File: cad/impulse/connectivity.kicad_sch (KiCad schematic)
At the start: 4 parts

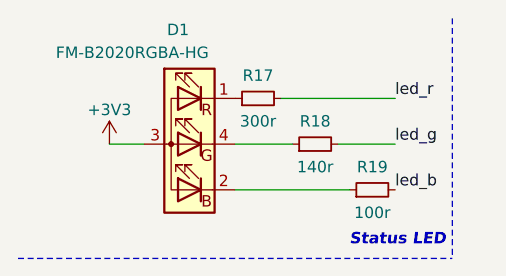
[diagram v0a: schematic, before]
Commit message: Transitioned to global labels when needed.
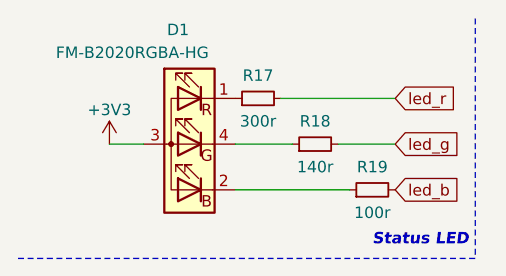
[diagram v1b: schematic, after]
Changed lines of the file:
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@@
     (stroke (width 0) (type default))
   )
-  (polyline (pts (xy 12.7 39.37) (xy 60.96 39.37))
+  (polyline (pts (xy 12.7 39.37) (xy 63.5 39.37))
     (stroke (width 0) (type dash))
   )
@@
     (stroke (width 0) (type default))
   )
-  (polyline (pts (xy 60.96 12.7) (xy 60.96 39.37))
+  (polyline (pts (xy 63.5 12.7) (xy 63.5 39.37))
     (stroke (width 0) (type dash))
   )
@@
     (stroke (width 0) (type default))
   )
-  (text "Status LED" (at 49.53 38.1 0)
+  (text "Status LED" (at 52.07 38.1 0)
     (effects (font (size 1.27 1.27) (thickness 0.254) bold italic) (justify left bottom))
   )
-  (label "led_g" (at 54.61 26.67 0) (fields_autoplaced)
-    (effects (font (size 1.27 1.27)) (justify left bottom))
+  (global_label "led_b" (shape input) (at 54.61 31.75 0) (fields_autoplaced)
+    (effects (font (size 1.27 1.27)) (justify left))
+    (property "Intersheetrefs" "${INTERSHEET_REFS}" (at 62.5352 31.75 0)
+      (effects (font (size 1.27 1.27)) (justify left) hide)
+    )
   )
-  (label "led_b" (at 54.61 31.75 0) (fields_autoplaced)
-    (effects (font (size 1.27 1.27)) (justify left bottom))
+  (global_label "led_g" (shape input) (at 54.61 26.67 0) (fields_autoplaced)
+    (effects (font (size 1.27 1.27)) (justify left))
+    (property "Intersheetrefs" "${INTERSHEET_REFS}" (at 62.5352 26.67 0)
+      (effects (font (size 1.27 1.27)) (justify left) hide)
+    )
   )
-  (label "led_r" (at 54.61 21.59 0) (fields_autoplaced)
-    (effects (font (size 1.27 1.27)) (justify left bottom))
+  (global_label "led_r" (shape input) (at 54.61 21.59 0) (fields_autoplaced)
+    (effects (font (size 1.27 1.27)) (justify left))
+    (property "Intersheetrefs" "${INTERSHEET_REFS}" (at 62.1724 21.59 0)
+      (effects (font (size 1.27 1.27)) (justify left) hide)
+    )
   )
   (symbol (lib_id "Device:R_Small") (at 52.07 31.75 90) (unit 1)

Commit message: Finished with LoRa.
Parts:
- added C15, C16, C35: 100n, symbol Device:C_Small
- added C17: 1n, symbol Device:C_Small
- added C18: 82p, symbol Device:C_Small
- added C19: 47n, symbol Device:C_Small
- added C20: 3p6, symbol Device:C_Small
- added C21, C28, C29, C33: 0f, symbol Device:C_Small
- added C22, C26: 100p, symbol Device:C_Small
- added C23, C30: 4p7, symbol Device:C_Small
- added C24: 12p, symbol Device:C_Small
- added C25: 8p2, symbol Device:C_Small
- added C27: 10n, symbol Device:C_Small
- added C31: 1p, symbol Device:C_Small
- added C32: 3p9, symbol Device:C_Small
- added C34: 470n, symbol Device:C_Small
- added C36, C37: C_Small, symbol Device:C_Small
- added J11: Micro_SD_Card, symbol Connector:Micro_SD_Card
- added J12: Conn_Coaxial, symbol Connector:Conn_Coaxial
- added L3: 56n, symbol Device:L_Small
- added L4: 8n2, symbol Device:L_Small
- added L5: 18n, symbol Device:L_Small
- added L6: 0n, symbol Device:L_Small
- added L7: 0h, symbol Device:L_Small
- added L8: 33n, symbol Device:L_Small
- added L9: 15u, symbol Device:L_Small
- added R25, R26, R27, R28: 10k, symbol Device:R_Small
- added R31: 100r, symbol Device:R_Small
- added U6: W25Q32JVSS, Package_SO:SOIC-8_5.23x5.23mm_P1.27mm, symbol Memory_Flash:W25Q32JVSS
- added U7: BGS12PL6, symbol impulse:BGS12PL6
- added U8: SX1268, symbol impulse:sx1268
- added Y1: 32MHZ, symbol Device:Crystal_GND24
- renumbered D1 to D6, R17 to R24, R18 to R29, R19 to R30
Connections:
- net +3V3: now also C15.1, C16.1, C27.1, C33.1, C35.1, J11.4 (VDD), L7.1, R25.1, R26.1, R27.1, R28.1, U6.8 (VCC), U7.4 (VDD), U8.1 (VDD_IN), U8.10 (VBAT), U8.11 (VBAT_IO)
- new net: C20.2, C24.1, L4.2, L5.1
- new net: C22.1, L5.2
- new net: C18.1, C19.1, L3.1, U8.24 (VR_PA)
- new net: C21.1, L3.2, U8.23 (RFO)
- new net: C20.1, C21.2, C23.1, L4.1
- new net: C34.1, L7.2, L9.1, U8.7 (VREG)
- new net: L9.2, U8.9 (DCC_SW)
- new net: C17.1, R31.2, U7.6 (CTRL)
- new net: C30.1, L8.1, U8.22 (RFI_N)
- new net: C32.1, L8.2, U8.21 (RFI_P)
- new net: C30.2, C31.1, U7.3 (RF1)
- new net: C26.2, C28.2, L6.1
- new net: C29.1, J12.1 (In), L6.2
- new net: C22.2, C25.1, U7.1 (RF2)
- new net: C26.1, U7.5 (RFIN)
- new net GND: C15.2, C16.2, C17.2, C18.2, C19.2, C23.2, C24.2, C25.2, C27.2, C28.1, C29.2, C31.2, C32.2, C33.2, C34.2, C35.2, C36.2, C37.2, J11.6 (VSS), J12.2 (Ext), U6.4 (GND), U7.2 (GND), U8.2 (GND), U8.20 (GND), U8.25 (GND), U8.5 (GND), U8.8 (GND), Y1.2, Y1.4
- new net SD_cs: J11.2 (DAT3/CD), R25.2
- new net SD_miso: J11.7 (DAT0), R28.2
- new net SD_mosi: J11.3 (CMD), R26.2
- new net SD_sck: J11.5 (CLK), R27.2
- new net flash_cs: U6.1 (~{CS})
- new net flash_miso: U6.2 (DO(IO1))
- new net flash_mosi: U6.5 (DI(IO0))
- new net flash_sck: U6.6 (CLK)
- new net sx_busy: U8.14 (BUSY)
- new net sx_dio_2: R31.1, U8.12 (DIO2)
- new net sx_miso: U8.16 (MISO)
- new net sx_mosi: U8.17 (MOSI)
- new net sx_nrst: U8.15 (NRESET)
- new net sx_nss: U8.19 (NSS)
- new net sx_sck: U8.18 (SCK)
- new net sx_xta: C37.1, U8.3 (XTA), Y1.3
- new net sx_xtb: C36.1, U8.4 (XTB), Y1.1
- no-connect marks 0 -> 7
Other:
- note added: "Flash Memory"
- note added: "LoRa Radio"
- note added: "SD Card"

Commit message: Finnished the design.
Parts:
- C36, C37: value C_Small -> 16p
- L6: value 0n -> 0h
- U6: footprint Package_SO:SOIC-8_5.23x5.23mm_P1.27mm -> (none)
- Y1: value 32MHZ -> XL7EL89COI-111YLC-32M
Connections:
- net sx_busy: no longer names the net of U8.14 (BUSY)
- net sx_nrst: no longer names the net of U8.15 (NRESET)
- no-connect marks 7 -> 9
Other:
- note added: "SPI1"
- note added: "SPI2"
- note added: "SPI3"
- company: (none) -> markbel
- title: (none) -> Connectivity
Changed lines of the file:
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@@
 (kicad_sch (version 20230121) (generator eeschema)
   (paper "A4")
+  (title_block
+    (title "Connectivity")
+    (company "markbel")
+  )
   (junction (at 128.27 91.44) (diameter 0) (color 0 0 0 0)
   )
@@
   )
   (no_connect (at 107.95 26.67))
+  (no_connect (at 106.68 109.22))
   (no_connect (at 107.95 44.45))
   (no_connect (at 31.75 60.96))
@@
   (no_connect (at 76.2 99.06))
   (no_connect (at 31.75 63.5))
+  (no_connect (at 106.68 111.76))
   (wire (pts (xy 229.87 85.09) (xy 233.68 85.09))
     (stroke (width 0) (type default))
@@
     (stroke (width 0) (type default))
   )
+  (text "SPI2" (at 58.42 74.93 0)
+    (effects (font (size 1.27 1.27) (thickness 0.254) bold italic) (justify left bottom))
+  )
+  (text "SPI3\n" (at 161.29 52.07 0)
+    (effects (font (size 1.27 1.27) (thickness 0.254) bold italic) (justify left bottom))
+  )
   (text "LoRa Radio" (at 273.05 109.22 0)
     (effects (font (size 1.27 1.27) (thickness 0.254) bold italic) (justify left bottom))
   )
   (text "Status LED" (at 52.07 38.1 0)
+    (effects (font (size 1.27 1.27) (thickness 0.254) bold italic) (justify left bottom))
+  )
+  (text "SPI1" (at 279.4 106.68 0)
     (effects (font (size 1.27 1.27) (thickness 0.254) bold italic) (justify left bottom))
   )
@@
     )
   )
-  (global_label "sx_busy" (shape input) (at 106.68 111.76 0) (fields_autoplaced)
-    (effects (font (size 1.27 1.27)) (justify left))
-    (property "Intersheetrefs" "${INTERSHEET_REFS}" (at 116.9033 111.76 0)
-      (effects (font (size 1.27 1.27)) (justify left) hide)
-    )
-  )
   (global_label "led_g" (shape input) (at 54.61 26.67 0) (fields_autoplaced)
     (effects (font (size 1.27 1.27)) (justify left))
@@
     )
   )
-  (global_label "sx_nrst" (shape input) (at 106.68 109.22 0) (fields_autoplaced)
-    (effects (font (size 1.27 1.27)) (justify left))
-    (property "Intersheetrefs" "${INTERSHEET_REFS}" (at 116.2986 109.22 0)
-      (effects (font (size 1.27 1.27)) (justify left) hide)
-    )
-  )
   (global_label "led_r" (shape input) (at 54.61 21.59 0) (fields_autoplaced)
     (effects (font (size 1.27 1.27)) (justify left))
@@
       (effects (font (size 1.27 1.27)) (justify left))
     )
-    (property "Footprint" "Package_SO:SOIC-8_5.23x5.23mm_P1.27mm" (at 41.91 58.42 0)
+    (property "Footprint" "" (at 41.91 58.42 0)
       (effects (font (size 1.27 1.27)) hide)
     )
@@
       (effects (font (size 1.27 1.27)) (justify left))
     )
-    (property "Value" "C_Small" (at 176.53 117.4813 0)
+    (property "Value" "16p" (at 176.53 117.4813 0)
       (effects (font (size 1.27 1.27)) (justify left))
     )
@@
   (symbol (lib_id "Device:Crystal_GND24") (at 166.37 113.03 0) (unit 1)
     (in_bom yes) (on_board yes) (dnp no)
-    (property "Reference" "Y1" (at 157.48 104.14 0)
-      (effects (font (size 1.27 1.27)))
-    )
-    (property "Value" "32MHZ" (at 157.48 106.68 0)
+    (property "Reference" "Y1" (at 160.02 106.68 0)
+      (effects (font (size 1.27 1.27)))
+    )
+    (property "Value" "XL7EL89COI-111YLC-32M " (at 149.86 109.22 0)
       (effects (font (size 1.27 1.27)))
     )
@@
       (effects (font (size 1.27 1.27)))
     )
-    (property "Value" "0n" (at 240.03 82.55 90)
+    (property "Value" "0h" (at 240.03 82.55 90)
       (effects (font (size 1.27 1.27)))
     )
@@
       (effects (font (size 1.27 1.27)) (justify left))
     )
-    (property "Value" "C_Small" (at 156.21 117.4813 0)
-      (effects (font (size 1.27 1.27)) (justify left))
-    )
+    (property "Value" "16p" (at 156.21 117.4813 0)
+      (effects (font (size 1.27 1.27)) (justify left))
+    )

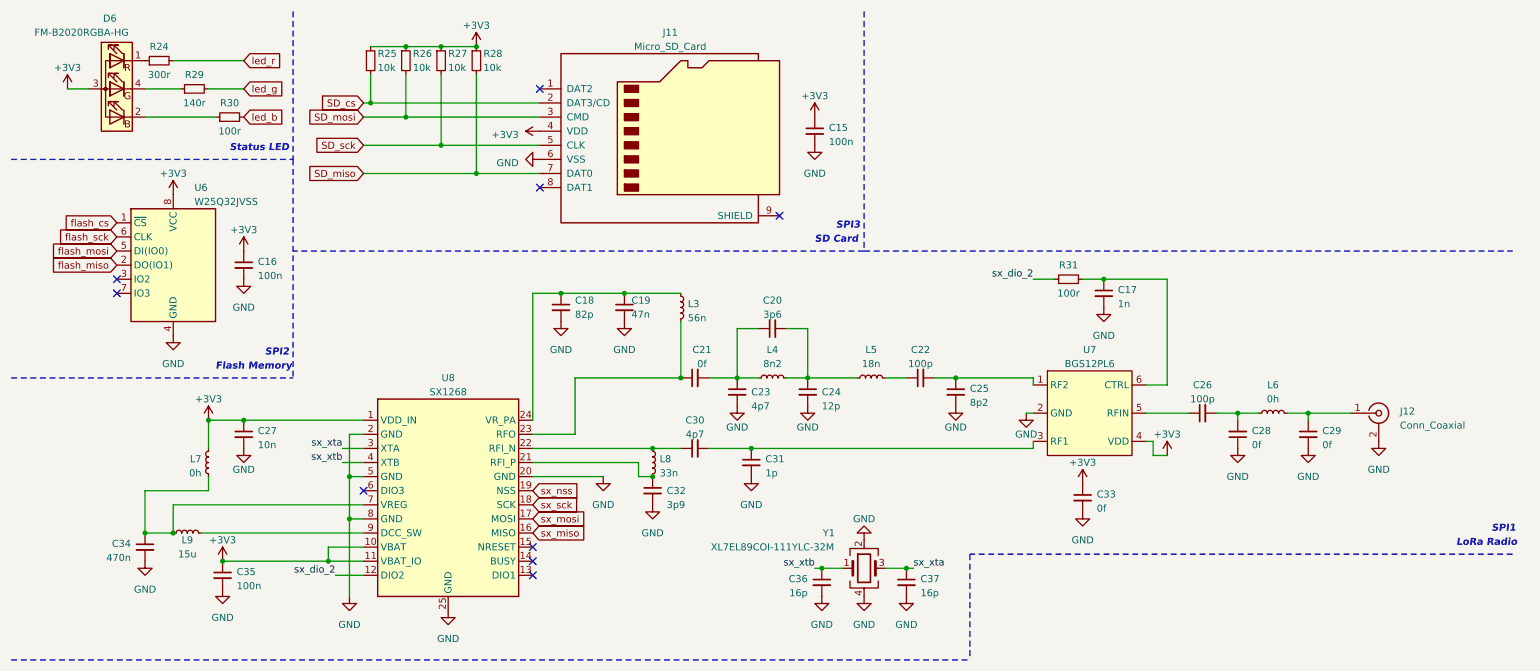
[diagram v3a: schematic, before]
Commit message: Started working on BOM, did consolidation.
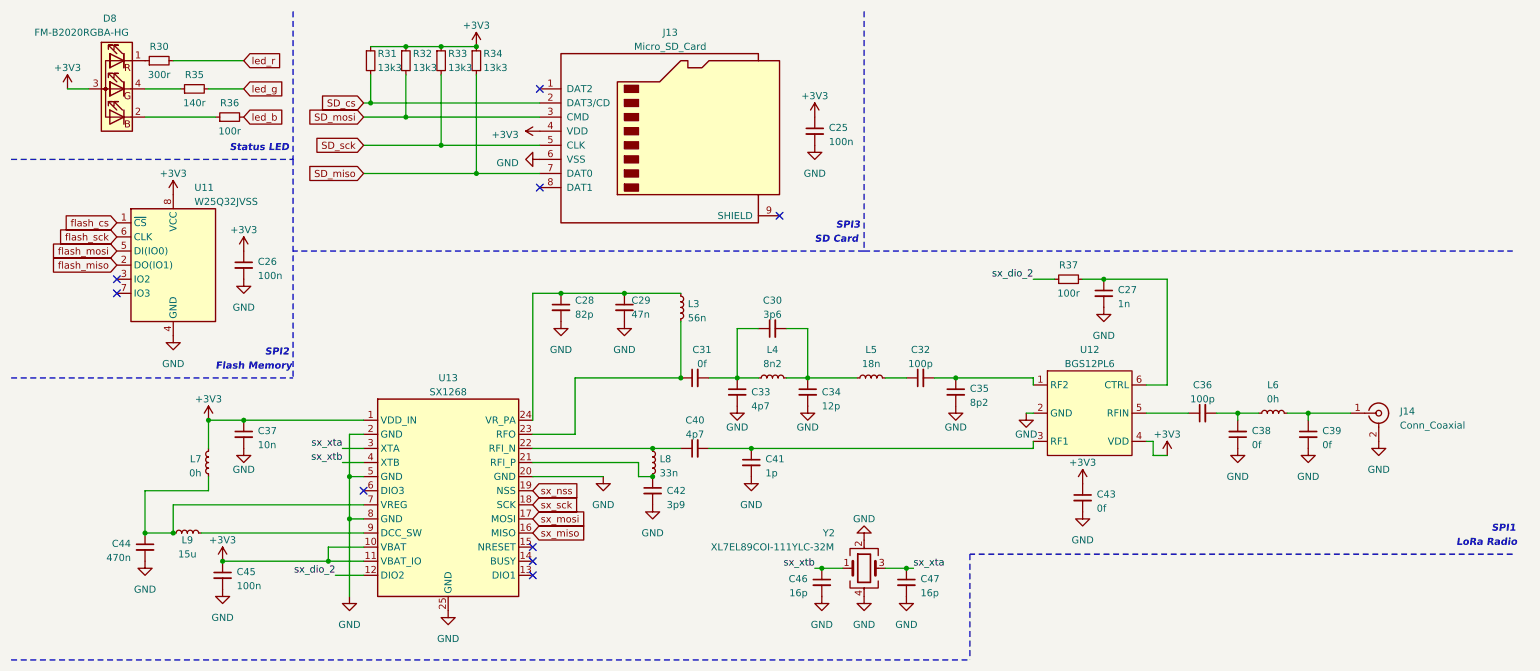
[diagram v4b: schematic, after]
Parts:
- C25: renamed from C15; lcsc (none) -> C1525
- C26: renamed from C16; lcsc (none) -> C1525
- C45: renamed from C35; lcsc (none) -> C1525
- C46: renamed from C36; lcsc (none) -> C5142569
- C47: renamed from C37; lcsc (none) -> C5142569
- D8: renamed from D6; lcsc (none) -> C108793
- J13: renamed from J11; lcsc (none) -> C393941
- J14: renamed from J12; lcsc (none) -> C5299419
- R30: renamed from R24; lcsc (none) -> C3017471
- R31: renamed from R25; value 10k -> 13k3; lcsc (none) -> C3015832
- R32: renamed from R26; value 10k -> 13k3; lcsc (none) -> C3015832
- R33: renamed from R27; value 10k -> 13k3; lcsc (none) -> C3015832
- R34: renamed from R28; value 10k -> 13k3; lcsc (none) -> C3015832
- R35: renamed from R29; lcsc (none) -> C3015963
- R36: renamed from R30; lcsc (none) -> C3152058
- R37: renamed from R31; lcsc (none) -> C3152058
- U11: renamed from U6; lcsc (none) -> C2834491
- U12: renamed from U7; lcsc (none) -> C2939943
- U13: renamed from U8; lcsc (none) -> C244368
- Y2: renamed from Y1; lcsc (none) -> C2965584
- renumbered C17 to C27, C18 to C28, C19 to C29, C20 to C30, C21 to C31, C22 to C32, C23 to C33, C24 to C34, C25 to C35, C26 to C36, C27 to C37, C28 to C38, C29 to C39, C30 to C40, C31 to C41, C32 to C42, C33 to C43, C34 to C44

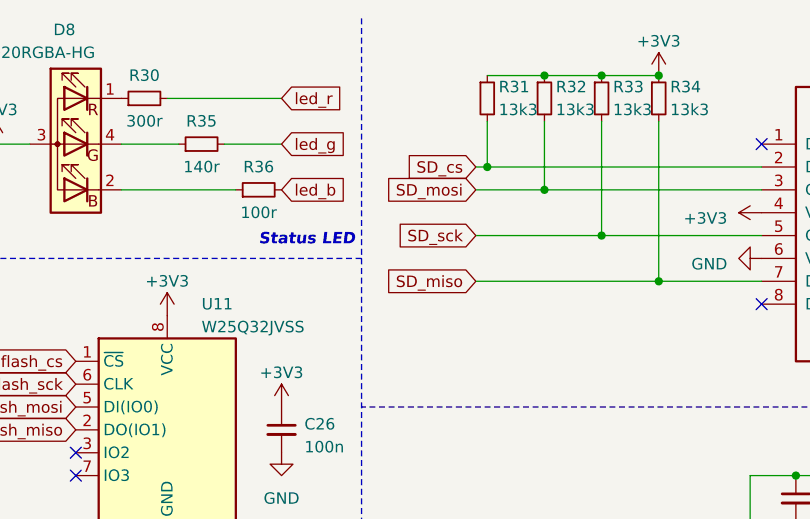
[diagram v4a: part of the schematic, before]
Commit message: Finished with schematic, starting to route traces.
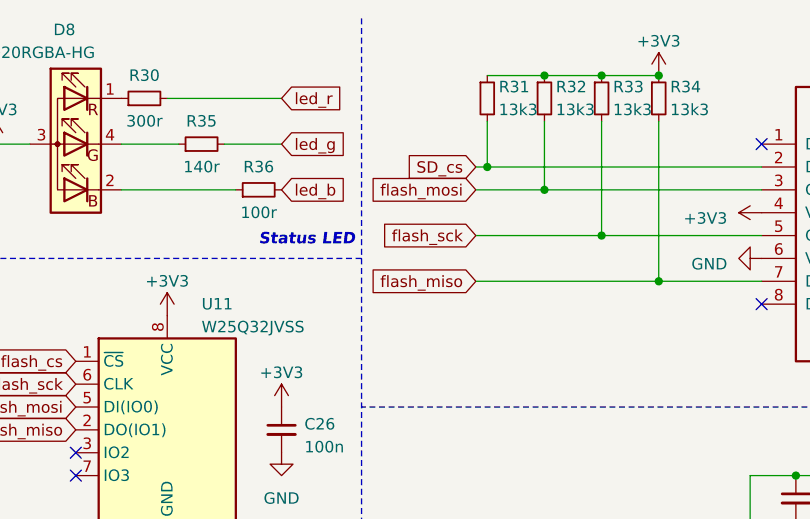
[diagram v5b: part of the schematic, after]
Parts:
- C25, C26, C31, C38, C39, C43, C45, C46, C47: footprint (none) -> Capacitor_SMD:C_0402_1005Metric
- C27: footprint (none) -> Capacitor_SMD:C_0402_1005Metric; lcsc (none) -> C53547
- C28: footprint (none) -> Capacitor_SMD:C_0402_1005Metric; lcsc (none) -> C525222
- C29: footprint (none) -> Capacitor_SMD:C_0402_1005Metric; lcsc (none) -> C5137574
- C30: footprint (none) -> Capacitor_SMD:C_0402_1005Metric; lcsc (none) -> C5186879
- C32, C36: footprint (none) -> Capacitor_SMD:C_0402_1005Metric; lcsc (none) -> C1546
- C33, C40: footprint (none) -> Capacitor_SMD:C_0402_1005Metric; lcsc (none) -> C482481
- C34: footprint (none) -> Capacitor_SMD:C_0402_1005Metric; lcsc (none) -> C1547
- C35: footprint (none) -> Capacitor_SMD:C_0603_1608Metric; lcsc (none) -> C5137629
- C37: footprint (none) -> Capacitor_SMD:C_0603_1608Metric; lcsc (none) -> C525264
- C41: footprint (none) -> Capacitor_SMD:C_0402_1005Metric; lcsc (none) -> C5137619
- C42: footprint (none) -> Capacitor_SMD:C_0402_1005Metric; lcsc (none) -> C696882
- C44: footprint (none) -> Capacitor_SMD:C_0402_1005Metric; lcsc (none) -> C5142573
- D8: footprint (none) -> LED_SMD:FM-B2020RGBA-HG
- J13: footprint (none) -> Connector_Card:microSD-Generic
- J14: footprint (none) -> Connector_Coaxial:U.FL_Hirose_U.FL-R-SMT-1_Vertical
- L3: footprint (none) -> Inductor_SMD:L_0402_1005Metric; lcsc (none) -> C90181
- L4: footprint (none) -> Inductor_SMD:L_0402_1005Metric; lcsc (none) -> C90138
- L5: footprint (none) -> Inductor_SMD:L_0402_1005Metric; lcsc (none) -> C395050
- L6, L7: footprint (none) -> Inductor_SMD:L_0402_1005Metric
- L8: footprint (none) -> Inductor_SMD:L_0402_1005Metric; lcsc (none) -> C381885
- L9: footprint (none) -> Inductor_SMD:L_0805_2012Metric; lcsc (none) -> C383402
- R30, R31, R32, R33, R34, R35, R36, R37: footprint (none) -> Resistor_SMD:R_0402_1005Metric
- U11: footprint (none) -> Package_SO:SOIC-8_5.23x5.23mm_P1.27mm
- U12: footprint (none) -> RF:BGS12PL6
- U13: footprint (none) -> Package_DFN_QFN:QFN-24-1EP_4x4mm_P0.5mm_EP2.7x2.7mm
- Y2: footprint (none) -> Crystal:Crystal_SMD_2016-4Pin_2.0x1.6mm
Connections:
- net SD_miso is gone; now on net flash_miso: J13.7 (DAT0), R34.2
- net SD_mosi is gone; now on net flash_mosi: J13.3 (CMD), R32.2
- net SD_sck is gone; now on net flash_sck: J13.5 (CLK), R33.2
